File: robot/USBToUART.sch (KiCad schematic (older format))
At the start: 1 part

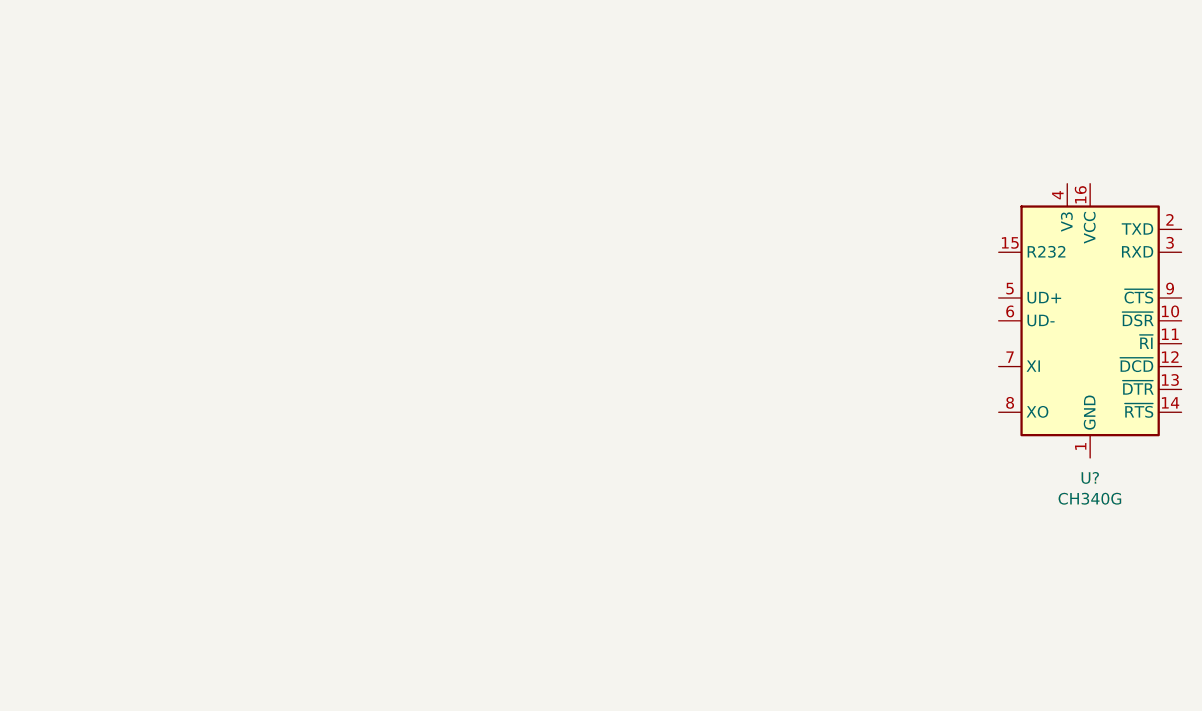
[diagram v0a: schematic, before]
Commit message: USB to UART + autoreset
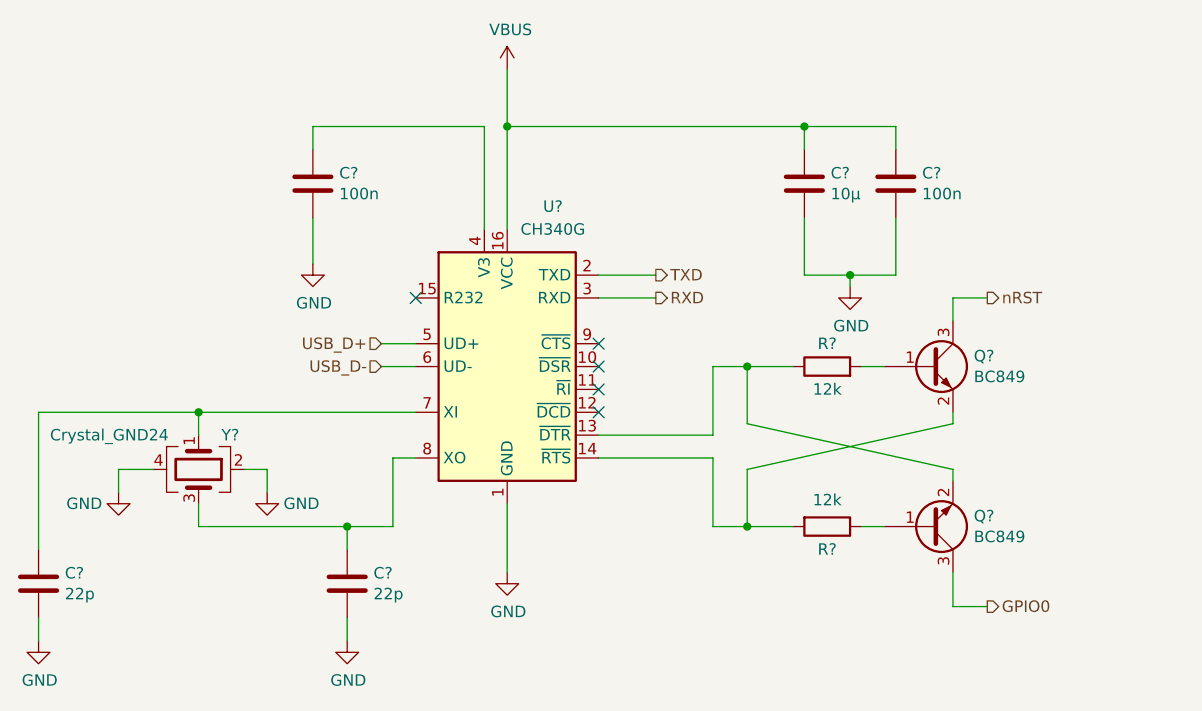
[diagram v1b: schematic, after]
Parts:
- added C? (x2): 100n, symbol Device:C
- added C?: 10µ, symbol Device:C
- added C? (x2): 22p, symbol Device:C
- added Q? (x2): BC849, Package_TO_SOT_SMD:SOT-23, symbol Transistor_BJT:BC849
- added R? (x2): 12k, symbol Device:R
- added Y?: Crystal_GND24, symbol Device:Crystal_GND24
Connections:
- net GND: now reaches U?.1 (GND)
- net GND: now also C?.2, C?.2, C?.2, C?.2, C?.2, Y?.2, Y?.4
- net at U?.13 (~DTR): now also Q?.2 (E), R?.1
- net at U?.14 (~RTS): now also Q?.2 (E), R?.2
- net VBUS: now reaches U?.16 (VCC)
- net VBUS: now also C?.1, C?.1
- net TXD: now reaches U?.2 (TXD)
- net RXD: now reaches U?.3 (RXD)
- net at U?.4 (V3): now also C?.1
- net USB_D+: now reaches U?.5 (UD+)
- net USB_D-: now reaches U?.6 (UD-)
- net at U?.7 (XI): now also C?.1, Y?.1
- net at U?.8 (XO): now also C?.1, Y?.3
- new net: Q?.1 (B), R?.2
- new net: Q?.1 (B), R?.1
- new net GPIO0: Q?.3 (C)
- new net nRST: Q?.3 (C)
- no-connect marks 0 -> 5
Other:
- moved on the sheet: U?

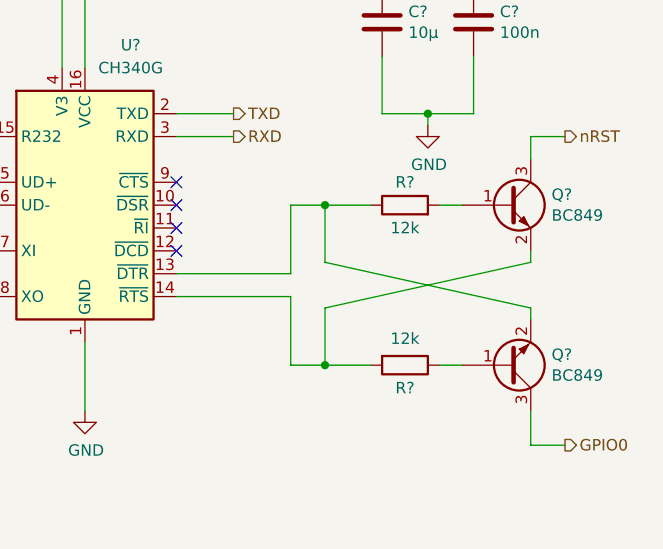
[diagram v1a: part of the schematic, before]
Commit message: added new core, changes to USBToUART
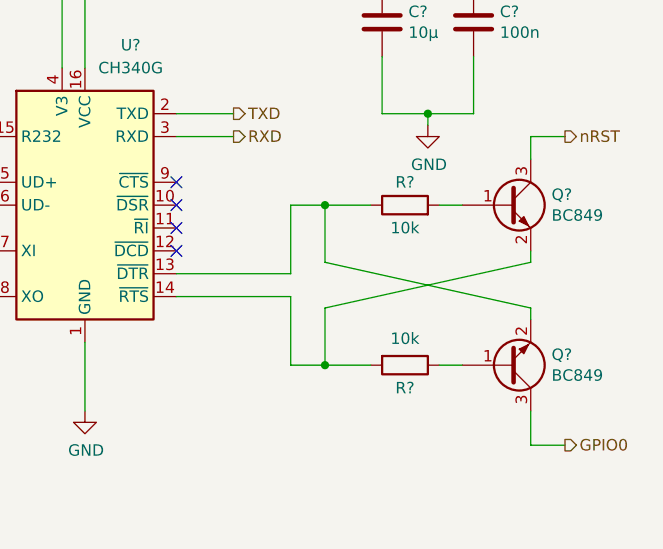
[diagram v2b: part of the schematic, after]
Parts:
- R? (x2): value 12k -> 10k
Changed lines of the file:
@@
 P 4850 3750
 F 0 "R?" V 4950 3750 50  0000 C CNN
-F 1 "12k" V 4750 3750 50  0000 C CNN
+F 1 "10k" V 4750 3750 50  0000 C CNN
 F 2 "" V 4780 3750 50  0001 C CNN
 F 3 "~" H 4850 3750 50  0001 C CNN
@@
 P 4850 4450
 F 0 "R?" V 4950 4450 50  0000 C CNN
-F 1 "12k" V 4734 4450 50  0000 C CNN
+F 1 "10k" V 4734 4450 50  0000 C CNN
 F 2 "" V 4780 4450 50  0001 C CNN
 F 3 "~" H 4850 4450 50  0001 C CNN
